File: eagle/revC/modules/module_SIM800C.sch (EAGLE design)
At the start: 10 parts, among them IC1 SIM800C, X1 734120110

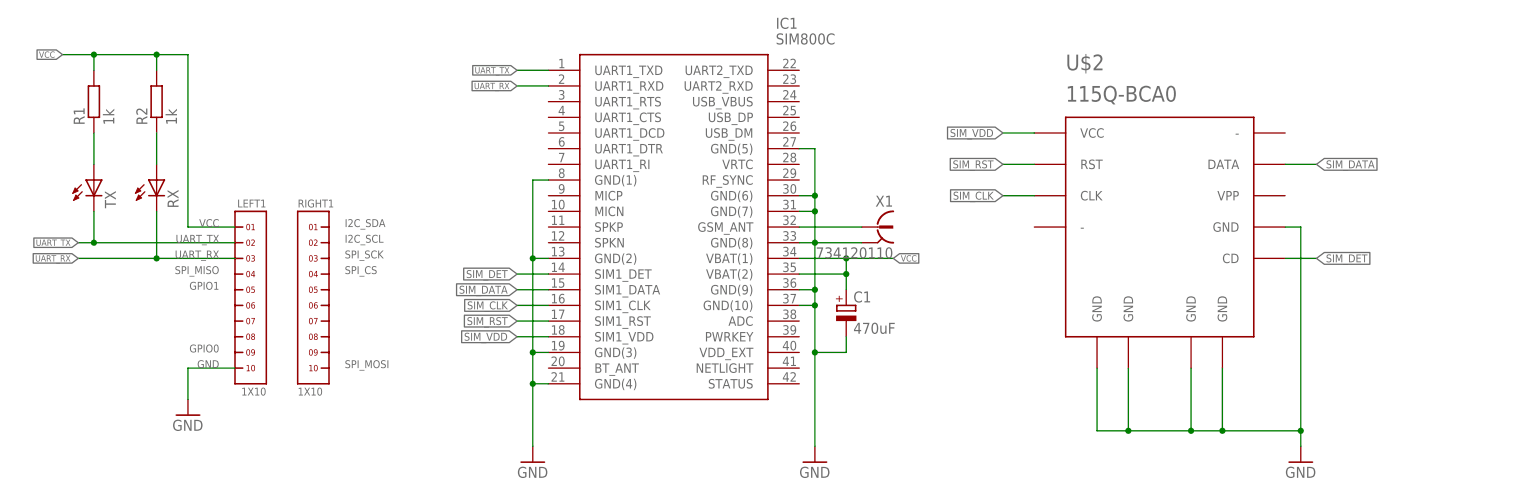
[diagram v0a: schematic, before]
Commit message: [SIM800C] Added PWRKEY connection
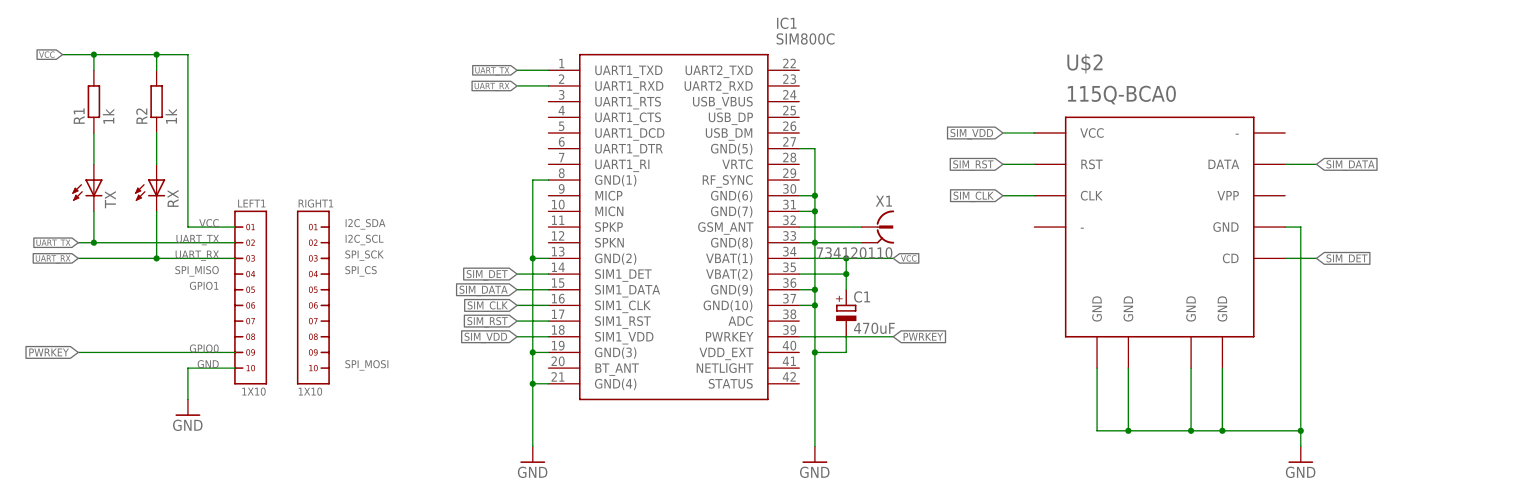
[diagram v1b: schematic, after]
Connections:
- new net PWRKEY: IC1.PWRKEY, LEFT1.9
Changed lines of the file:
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@@
+</segment>
+</net>
+<net name="PWRKEY" class="0">
+<segment>
+<pinref part="LEFT1" gate="G$1" pin="9"/>
+<wire x1="35.56" y1="20.32" x2="10.16" y2="20.32" width="0.1524" layer="91"/>
+<label x="10.16" y="20.32" size="1.27" layer="95" rot="R180" xref="yes"/>
+</segment>
+<segment>
+<pinref part="IC1" gate="G$1" pin="PWRKEY"/>
+<wire x1="127" y1="22.86" x2="142.24" y2="22.86" width="0.1524" layer="91"/>
+<label x="142.24" y="22.86" size="1.27" layer="95" xref="yes"/>
 </segment>
 </net>

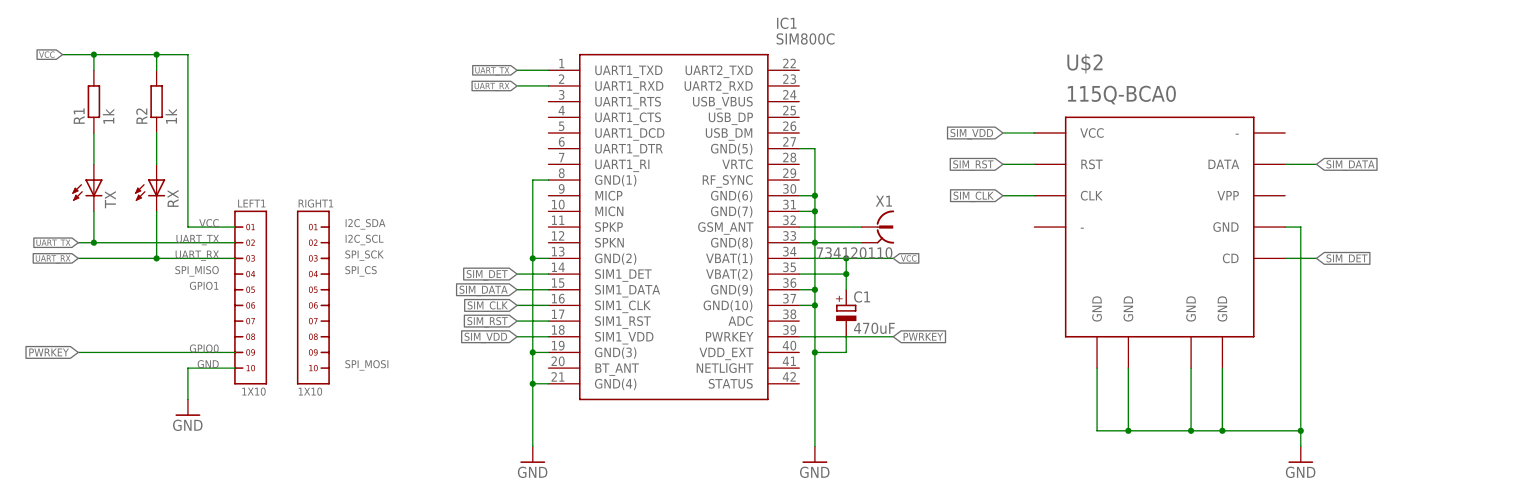
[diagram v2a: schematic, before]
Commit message: [SIM800] Added SIM detection pullup
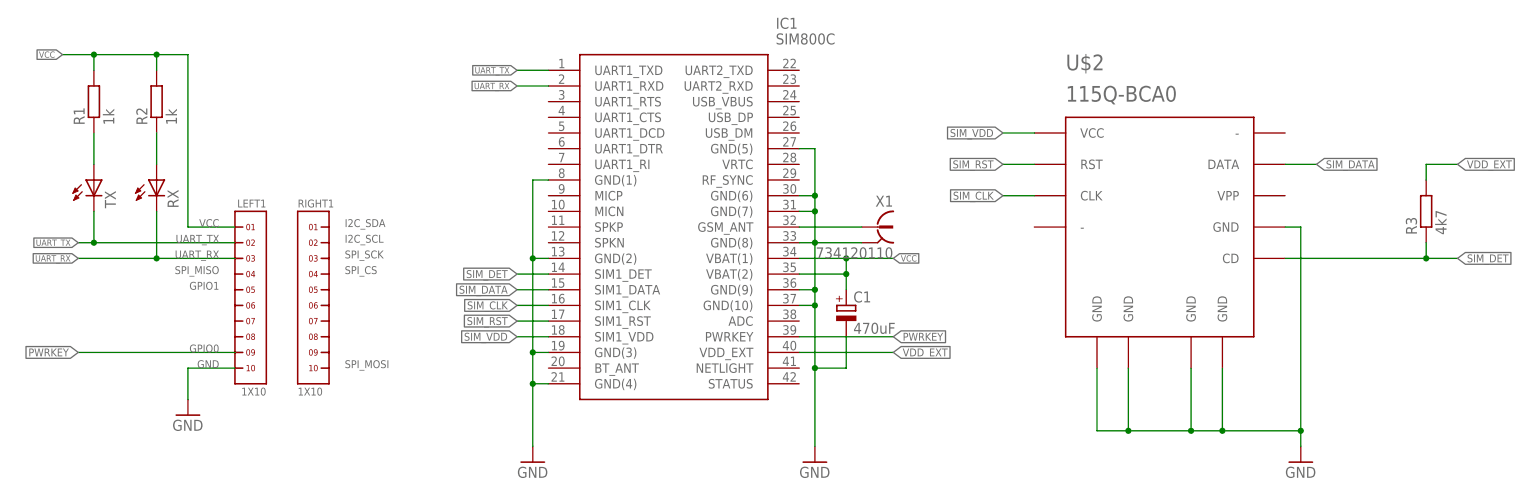
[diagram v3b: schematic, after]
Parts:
- added R3: 4k7, rcl:R-EU_R0603
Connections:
- new net VDD_EXT: IC1.VDD_EXT, R3.2
- net SIM_DET: now also R3.1
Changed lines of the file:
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@@
 <part name="U$2" library="con-sim" deviceset="115Q-BCA0" device=""/>
 <part name="GND4" library="supply1" library_urn="urn:adsk.eagle:library:371" deviceset="GND" device=""/>
+<part name="R3" library="rcl" library_urn="urn:adsk.eagle:library:334" deviceset="R-EU_" device="R0603" package3d_urn="urn:adsk.eagle:package:23555/2" value="4k7"/>
 </parts>
 <sheets>
@@
 <instance part="U$2" gate="G$1" x="185.42" y="43.18"/>
 <instance part="GND4" gate="1" x="208.28" y="2.54"/>
+<instance part="R3" gate="G$1" x="228.6" y="43.18" rot="R90"/>
 </instances>
 <busses>
@@
 <pinref part="GND1" gate="1" pin="GND"/>
 <wire x1="129.54" y1="38.1" x2="127" y2="38.1" width="0.1524" layer="91"/>
-<wire x1="129.54" y1="5.08" x2="129.54" y2="20.32" width="0.1524" layer="91"/>
+<wire x1="129.54" y1="5.08" x2="129.54" y2="17.78" width="0.1524" layer="91"/>
 <junction x="129.54" y="38.1"/>
 <pinref part="IC1" gate="G$1" pin="GND(10)"/>
-<wire x1="129.54" y1="20.32" x2="129.54" y2="27.94" width="0.1524" layer="91"/>
+<wire x1="129.54" y1="17.78" x2="129.54" y2="27.94" width="0.1524" layer="91"/>
 <wire x1="129.54" y1="27.94" x2="129.54" y2="30.48" width="0.1524" layer="91"/>
 <wire x1="129.54" y1="30.48" x2="129.54" y2="38.1" width="0.1524" layer="91"/>
@@
 <wire x1="129.54" y1="53.34" x2="129.54" y2="45.72" width="0.1524" layer="91"/>
 <junction x="129.54" y="45.72"/>
-<wire x1="134.62" y1="22.86" x2="134.62" y2="20.32" width="0.1524" layer="91"/>
-<wire x1="134.62" y1="20.32" x2="129.54" y2="20.32" width="0.1524" layer="91"/>
-<junction x="129.54" y="20.32"/>
+<wire x1="134.62" y1="22.86" x2="134.62" y2="17.78" width="0.1524" layer="91"/>
+<wire x1="134.62" y1="17.78" x2="129.54" y2="17.78" width="0.1524" layer="91"/>
+<junction x="129.54" y="17.78"/>
 <pinref part="C1" gate="G$1" pin="-"/>
 </segment>
@@
 <segment>
 <pinref part="U$2" gate="G$1" pin="CD"/>
-<wire x1="210.82" y1="35.56" x2="205.74" y2="35.56" width="0.1524" layer="91"/>
-<label x="210.82" y="35.56" size="1.27" layer="95" xref="yes"/>
+<wire x1="233.68" y1="35.56" x2="228.6" y2="35.56" width="0.1524" layer="91"/>
+<label x="233.68" y="35.56" size="1.27" layer="95" xref="yes"/>
+<pinref part="R3" gate="G$1" pin="1"/>
+<wire x1="228.6" y1="35.56" x2="205.74" y2="35.56" width="0.1524" layer="91"/>
+<wire x1="228.6" y1="35.56" x2="228.6" y2="38.1" width="0.1524" layer="91"/>
+<junction x="228.6" y="35.56"/>
 </segment>
 <segment>
@@
 </segment>
 </net>
+<net name="VDD_EXT" class="0">
+<segment>
+<pinref part="IC1" gate="G$1" pin="VDD_EXT"/>
+<wire x1="127" y1="20.32" x2="142.24" y2="20.32" width="0.1524" layer="91"/>
+<label x="142.24" y="20.32" size="1.27" layer="95" xref="yes"/>
+</segment>
+<segment>
+<pinref part="R3" gate="G$1" pin="2"/>
+<wire x1="228.6" y1="48.26" x2="228.6" y2="50.8" width="0.1524" layer="91"/>
+<wire x1="228.6" y1="50.8" x2="233.68" y2="50.8" width="0.1524" layer="91"/>
+<label x="233.68" y="50.8" size="1.27" layer="95" xref="yes"/>
+</segment>
+</net>

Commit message: Replaced modules with library parts
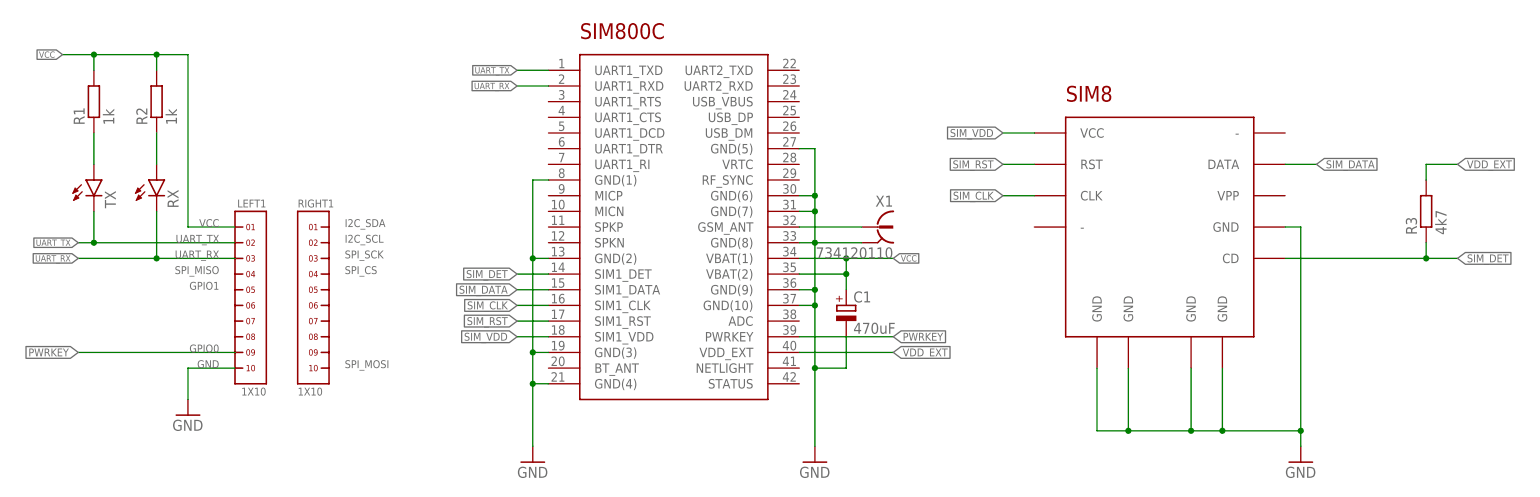
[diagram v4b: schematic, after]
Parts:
- IC1: device sim800c:SIM800C -> RadioShield:SIM800C
- U$2: device con-sim:115Q-BCA0 -> RadioShield:115Q-BCA0
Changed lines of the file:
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@@
 <?xml version="1.0" encoding="utf-8"?>
 <!DOCTYPE eagle SYSTEM "eagle.dtd">
-<eagle version="9.0.1">
+<eagle version="9.4.1">
 <drawing>
 <settings>
@@
 <part name="RIGHT1" library="headers(2mm)" deviceset="1X10" device=""/>
 <part name="X1" library="con-coax" library_urn="urn:adsk.eagle:library:133" deviceset="734120110" device="" package3d_urn="urn:adsk.eagle:package:6199/1"/>
-<part name="IC1" library="sim800c" deviceset="SIM800C" device=""/>
+<part name="IC1" library="RadioShield" deviceset="SIM800C" device=""/>
 <part name="GND1" library="supply1" library_urn="urn:adsk.eagle:library:371" deviceset="GND" device=""/>
 <part name="GND2" library="supply1" library_urn="urn:adsk.eagle:library:371" deviceset="GND" device=""/>
 <part name="GND3" library="supply1" library_urn="urn:adsk.eagle:library:371" deviceset="GND" device=""/>
-<part name="R1" library="rcl" library_urn="urn:adsk.eagle:library:334" deviceset="R-EU_" device="R0603" package3d_urn="urn:adsk.eagle:package:23555/2" value="1k"/>
-<part name="R2" library="rcl" library_urn="urn:adsk.eagle:library:334" deviceset="R-EU_" device="R0603" package3d_urn="urn:adsk.eagle:package:23555/2" value="1k"/>
+<part name="R1" library="rcl" library_urn="urn:adsk.eagle:library:334" deviceset="R-EU_" device="R0603" package3d_urn="urn:adsk.eagle:package:23555/3" value="1k"/>
+<part name="R2" library="rcl" library_urn="urn:adsk.eagle:library:334" deviceset="R-EU_" device="R0603" package3d_urn="urn:adsk.eagle:package:23555/3" value="1k"/>
 <part name="TX" library="led" library_urn="urn:adsk.eagle:library:259" deviceset="LED" device="CHIPLED_0603" package3d_urn="urn:adsk.eagle:package:15822/2"/>
 <part name="RX" library="led" library_urn="urn:adsk.eagle:library:259" deviceset="LED" device="CHIPLED_0603" package3d_urn="urn:adsk.eagle:package:15822/2"/>
-<part name="C1" library="rcl" library_urn="urn:adsk.eagle:library:334" deviceset="CPOL-EU" device="SMCD" package3d_urn="urn:adsk.eagle:package:23434/1" value="470uF"/>
-<part name="U$2" library="con-sim" deviceset="115Q-BCA0" device=""/>
+<part name="C1" library="rcl" library_urn="urn:adsk.eagle:library:334" deviceset="CPOL-EU" device="SMCD" package3d_urn="urn:adsk.eagle:package:25923/2" value="470uF"/>
+<part name="U$2" library="RadioShield" deviceset="115Q-BCA0" device=""/>
 <part name="GND4" library="supply1" library_urn="urn:adsk.eagle:library:371" deviceset="GND" device=""/>
-<part name="R3" library="rcl" library_urn="urn:adsk.eagle:library:334" deviceset="R-EU_" device="R0603" package3d_urn="urn:adsk.eagle:package:23555/2" value="4k7"/>
+<part name="R3" library="rcl" library_urn="urn:adsk.eagle:library:334" deviceset="R-EU_" device="R0603" package3d_urn="urn:adsk.eagle:package:23555/3" value="4k7"/>
 </parts>
 <sheets>
@@
 </plain>
 <instances>
-<instance part="LEFT1" gate="G$1" x="38.1" y="27.94" rot="MR0"/>
-<instance part="RIGHT1" gate="G$1" x="48.26" y="27.94"/>
-<instance part="X1" gate="G$1" x="139.7" y="40.64" rot="MR0"/>
-<instance part="IC1" gate="G$1" x="86.36" y="66.04"/>
-<instance part="GND1" gate="1" x="129.54" y="2.54"/>
-<instance part="GND2" gate="1" x="83.82" y="2.54"/>
-<instance part="GND3" gate="1" x="27.94" y="10.16"/>
-<instance part="R1" gate="G$1" x="12.7" y="60.96" rot="R90"/>
-<instance part="R2" gate="G$1" x="22.86" y="60.96" rot="R90"/>
-<instance part="TX" gate="G$1" x="12.7" y="48.26"/>
-<instance part="RX" gate="G$1" x="22.86" y="48.26"/>
-<instance part="C1" gate="G$1" x="134.62" y="27.94"/>
-<instance part="U$2" gate="G$1" x="185.42" y="43.18"/>
-<instance part="GND4" gate="1" x="208.28" y="2.54"/>
-<instance part="R3" gate="G$1" x="228.6" y="43.18" rot="R90"/>
+<instance part="LEFT1" gate="G$1" x="38.1" y="27.94" smashed="yes" rot="MR0">
+<attribute name="NAME" x="40.64" y="43.815" size="1.27" layer="95" font="vector" rot="MR0"/>
+<attribute name="VALUE" x="40.64" y="13.335" size="1.27" layer="96" font="vector" rot="MR0"/>
+</instance>
+<instance part="RIGHT1" gate="G$1" x="48.26" y="27.94" smashed="yes">
+<attribute name="NAME" x="45.72" y="43.815" size="1.27" layer="95" font="vector"/>
+<attribute name="VALUE" x="45.72" y="13.335" size="1.27" layer="96" font="vector"/>
+</instance>
+<instance part="X1" gate="G$1" x="139.7" y="40.64" smashed="yes" rot="MR0">
+<attribute name="VALUE" x="142.24" y="35.56" size="1.778" layer="96" rot="MR0"/>
+<attribute name="NAME" x="142.24" y="43.942" size="1.778" layer="95" rot="MR0"/>
+</instance>
+<instance part="IC1" gate="G$1" x="106.68" y="43.18" smashed="yes"/>
+<instance part="GND1" gate="1" x="129.54" y="2.54" smashed="yes">
+<attribute name="VALUE" x="127" y="0" size="1.778" layer="96"/>
+</instance>
+<instance part="GND2" gate="1" x="83.82" y="2.54" smashed="yes">
+<attribute name="VALUE" x="81.28" y="0" size="1.778" layer="96"/>
+</instance>
+<instance part="GND3" gate="1" x="27.94" y="10.16" smashed="yes">
+<attribute name="VALUE" x="25.4" y="7.62" size="1.778" layer="96"/>
+</instance>
+<instance part="R1" gate="G$1" x="12.7" y="60.96" smashed="yes" rot="R90">
+<attribute name="NAME" x="11.2014" y="57.15" size="1.778" layer="95" rot="R90"/>
+<attribute name="VALUE" x="16.002" y="57.15" size="1.778" layer="96" rot="R90"/>
+</instance>
+<instance part="R2" gate="G$1" x="22.86" y="60.96" smashed="yes" rot="R90">
+<attribute name="NAME" x="21.3614" y="57.15" size="1.778" layer="95" rot="R90"/>
+<attribute name="VALUE" x="26.162" y="57.15" size="1.778" layer="96" rot="R90"/>
+</instance>
+<instance part="TX" gate="G$1" x="12.7" y="48.26" smashed="yes">
+<attribute name="NAME" x="16.256" y="43.688" size="1.778" layer="95" rot="R90"/>
+<attribute name="VALUE" x="18.415" y="43.688" size="1.778" layer="96" rot="R90"/>
+</instance>
+<instance part="RX" gate="G$1" x="22.86" y="48.26" smashed="yes">
+<attribute name="NAME" x="26.416" y="43.688" size="1.778" layer="95" rot="R90"/>
+<attribute name="VALUE" x="28.575" y="43.688" size="1.778" layer="96" rot="R90"/>
+</instance>
+<instance part="C1" gate="G$1" x="134.62" y="27.94" smashed="yes">
+<attribute name="NAME" x="135.763" y="28.4226" size="1.778" layer="95"/>
+<attribute name="VALUE" x="135.763" y="23.3426" size="1.778" layer="96"/>
+</instance>
+<instance part="U$2" gate="G$1" x="185.42" y="43.18" smashed="yes"/>
+<instance part="GND4" gate="1" x="208.28" y="2.54" smashed="yes">
+<attribute name="VALUE" x="205.74" y="0" size="1.778" layer="96"/>
+</instance>
+<instance part="R3" gate="G$1" x="228.6" y="43.18" smashed="yes" rot="R90">
+<attribute name="NAME" x="227.1014" y="39.37" size="1.778" layer="95" rot="R90"/>
+<attribute name="VALUE" x="231.902" y="39.37" size="1.778" layer="96" rot="R90"/>
+</instance>
 </instances>
 <busses>
